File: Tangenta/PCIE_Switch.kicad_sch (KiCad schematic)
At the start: 99 parts, among them U15 PI7C9X2G404SLBFDEX, U17 M24C04-RMN6TP

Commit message: ...
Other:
- note removed: "Do not populate initially!"
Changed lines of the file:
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@@
     (effects (font (size 1.27 1.27)) (justify right bottom))
-  )
-  (text "Do not populate initially!" (at 27.305 196.215 0)
-    (effects (font (size 1.27 1.27)) (justify left bottom))
   )
   (text "|\n|\n|\n|" (at 295.91 139.7 0)

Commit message: Schematic improvements.
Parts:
- added J15: Conn_01x06_Pin, Connector_PinHeader_1.00mm:PinHeader_1x06_P1.00mm_Vertical, symbol Connector:Conn_01x06_Pin
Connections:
- net GNDREF: now also J15.1 (Pin_1)
- net PCIE_SW_TCK: now also J15.2 (Pin_2)
- net PCIE_SW_TDI: now also J15.3 (Pin_3)
- net PCIE_SW_TDO: now also J15.4 (Pin_4)
- net PCIE_SW_TMS: now also J15.5 (Pin_5)
- net PCIE_SW_TRST_L: now also J15.6 (Pin_6)
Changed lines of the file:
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@@
     (stroke (width 0) (type default))
   )
+  (wire (pts (xy 34.29 97.155) (xy 57.15 97.155))
+    (stroke (width 0) (type default))
+  )
   (wire (pts (xy 35.56 135.255) (xy 18.415 135.255))
     (stroke (width 0) (type default))
@@
     (stroke (width 0) (type default))
   )
+  (wire (pts (xy 34.29 102.235) (xy 57.15 102.235))
+    (stroke (width 0) (type default))
+  )
   (wire (pts (xy 382.905 223.52) (xy 400.05 223.52))
     (stroke (width 0) (type default))
@@
     (stroke (width 0) (type default))
   )
-  (wire (pts (xy 233.68 161.29) (xy 248.92 161.29))
+  (wire (pts (xy 34.29 99.695) (xy 57.15 99.695))
     (stroke (width 0) (type default))
   )
-  (wire (pts (xy 180.34 218.44) (xy 165.1 218.44))
+  (wire (pts (xy 233.68 161.29) (xy 248.92 161.29))
     (stroke (width 0) (type default))
   )
-  (wire (pts (xy 57.15 99.06) (xy 34.29 99.06))
+  (wire (pts (xy 180.34 218.44) (xy 165.1 218.44))
     (stroke (width 0) (type default))
   )
@@
     (stroke (width 0) (type default))
   )
-  (wire (pts (xy 57.15 91.44) (xy 34.29 91.44))
-    (stroke (width 0) (type default))
-  )
   (wire (pts (xy 363.22 93.98) (xy 363.22 96.52))
     (stroke (width 0) (type default))
@@
     (stroke (width 0) (type default))
   )
+  (wire (pts (xy 34.29 92.075) (xy 57.15 92.075))
+    (stroke (width 0) (type default))
+  )
   (wire (pts (xy 35.56 264.795) (xy 18.415 264.795))
     (stroke (width 0) (type default))
@@
     (stroke (width 0) (type default))
   )
-  (wire (pts (xy 57.15 93.98) (xy 34.29 93.98))
-    (stroke (width 0) (type default))
-  )
   (wire (pts (xy 379.73 115.57) (xy 379.73 118.11))
     (stroke (width 0) (type default))
@@
     (stroke (width 0) (type default))
   )
+  (wire (pts (xy 34.29 104.775) (xy 57.15 104.775))
+    (stroke (width 0) (type default))
+  )
   (wire (pts (xy 213.36 267.97) (xy 232.41 267.97))
     (stroke (width 0) (type default))
@@
     (stroke (width 0) (type default))
   )
-  (wire (pts (xy 57.15 101.6) (xy 34.29 101.6))
-    (stroke (width 0) (type default))
-  )
   (wire (pts (xy 18.415 177.165) (xy 35.56 177.165))
     (stroke (width 0) (type default))
@@
     (stroke (width 0) (type default))
   )
-  (wire (pts (xy 57.15 96.52) (xy 34.29 96.52))
-    (stroke (width 0) (type default))
-  )
   (wire (pts (xy 180.34 139.7) (xy 165.1 139.7))
     (stroke (width 0) (type default))
@@
     (stroke (width 0) (type default))
   )
+  (wire (pts (xy 34.29 94.615) (xy 57.15 94.615))
+    (stroke (width 0) (type default))
+  )
   (wire (pts (xy 389.89 22.86) (xy 389.89 25.4))
     (stroke (width 0) (type default))
@@
     (effects (font (size 1.27 1.27)) (justify right bottom))
   )
-  (label "PCIE_SW_TRST_L" (at 57.15 101.6 180) (fields_autoplaced)
+  (label "PCIE_SW_TRST_L" (at 57.15 104.775 180) (fields_autoplaced)
     (effects (font (size 1.27 1.27)) (justify right bottom))
   )
@@
     (effects (font (size 1.27 1.27)) (justify left bottom))
   )
+  (label "GND" (at 57.15 92.075 180) (fields_autoplaced)
+    (effects (font (size 1.27 1.27)) (justify right bottom))
+  )
   (label "1V0" (at 318.77 93.98 0) (fields_autoplaced)
     (effects (font (size 1.27 1.27)) (justify left bottom))
@@
     (effects (font (size 1.27 1.27)) (justify left bottom))
   )
-  (label "PCIE_SW_TCK" (at 57.15 91.44 180) (fields_autoplaced)
+  (label "PCIE_SW_TCK" (at 57.15 94.615 180) (fields_autoplaced)
     (effects (font (size 1.27 1.27)) (justify right bottom))
   )
@@
     (effects (font (size 1.27 1.27)) (justify left bottom))
   )
-  (label "PCIE_SW_TDO" (at 57.15 96.52 180) (fields_autoplaced)
+  (label "PCIE_SW_TDO" (at 57.15 99.695 180) (fields_autoplaced)
     (effects (font (size 1.27 1.27)) (justify right bottom))
   )
@@
     (effects (font (size 1.27 1.27)) (justify left bottom))
   )
-  (label "PCIE_SW_TMS" (at 57.15 99.06 180) (fields_autoplaced)
+  (label "PCIE_SW_TMS" (at 57.15 102.235 180) (fields_autoplaced)
     (effects (font (size 1.27 1.27)) (justify right bottom))
   )
@@
     (effects (font (size 1.27 1.27)) (justify left bottom))
   )
-  (label "PCIE_SW_TDI" (at 57.15 93.98 180) (fields_autoplaced)
+  (label "PCIE_SW_TDI" (at 57.15 97.155 180) (fields_autoplaced)
     (effects (font (size 1.27 1.27)) (justify right bottom))
   )
@@
     (effects (font (size 1.27 1.27)) (justify left bottom))
   )
-  (hierarchical_label "PCIE_SW_TDO" (shape input) (at 34.29 96.52 180) (fields_autoplaced)
-    (effects (font (size 1.27 1.27)) (justify right))
-  )
   (hierarchical_label "PCIE1_CLK_N" (shape output) (at 386.715 139.7 0) (fields_autoplaced)
     (effects (font (size 1.27 1.27)) (justify left))
@@
     (effects (font (size 1.27 1.27)) (justify left))
   )
-  (hierarchical_label "PCIE_SW_TCK" (shape input) (at 34.29 91.44 180) (fields_autoplaced)
-    (effects (font (size 1.27 1.27)) (justify right))
-  )
   (hierarchical_label "PCIE3_PRSNT" (shape output) (at 386.715 190.5 0) (fields_autoplaced)
     (effects (font (size 1.27 1.27)) (justify left))
@@
     (effects (font (size 1.27 1.27)) (justify left))
   )
-  (hierarchical_label "PCIE_SW_TMS" (shape input) (at 34.29 99.06 180) (fields_autoplaced)
-    (effects (font (size 1.27 1.27)) (justify right))
-  )
   (hierarchical_label "PCIE2_CLK_N" (shape output) (at 386.715 168.91 0) (fields_autoplaced)
     (effects (font (size 1.27 1.27)) (justify left))
@@
     (effects (font (size 1.27 1.27)) (justify left))
   )
-  (hierarchical_label "PCIE_SW_TDI" (shape input) (at 34.29 93.98 180) (fields_autoplaced)
-    (effects (font (size 1.27 1.27)) (justify right))
-  )
-  (hierarchical_label "PCIE_SW_TRST_L" (shape input) (at 34.29 101.6 180) (fields_autoplaced)
-    (effects (font (size 1.27 1.27)) (justify right))
-  )
   (hierarchical_label "PCIE_RX_P" (shape input) (at 34.29 73.66 180) (fields_autoplaced)
     (effects (font (size 1.27 1.27)) (justify right))
@@
         )
       )
+    )
+  )
+  (symbol (lib_id "Connector:Conn_01x06_Pin") (at 29.21 97.155 0) (unit 1)
+    (in_bom yes) (on_board yes) (dnp no)
+    (property "Reference" "J15" (at 26.289 98.298 0)
+      (effects (font (size 1.27 1.27)))
+    )
+    (property "Value" "Conn_01x06_Pin" (at 29.845 89.535 0)
+      (effects (font (size 1.27 1.27)) hide)
+    )
+    (property "Footprint" "Connector_PinHeader_1.00mm:PinHeader_1x06_P1.00mm_Vertical" (at 29.21 97.155 0)
+      (effects (font (size 1.27 1.27)) hide)
+    )
+    (property "Datasheet" "~" (at 29.21 97.155 0)
+      (effects (font (size 1.27 1.27)) hide)
+    )
+    (pin "1")
+    (pin "2")
+    (pin "3")
+    (pin "4")
+    (pin "5")
+    (pin "6")
+    (instances
+      (project "Tangenta"
+        (path "/358d1bcf-7599-4352-8c4d-baa18a5f09e6/db297b0b-35f2-4e86-892c-83973f1ac2db"
+          (reference "J15") (unit 1)
+        )
+        (path "/358d1bcf-7599-4352-8c4d-baa18a5f09e6/9b1f6f94-444c-4c59-8de9-290bde336856/04648235-6c5e-4915-ab80-8fea22048f3c"
+          (reference "J15") (unit 1)
+        )
+      )

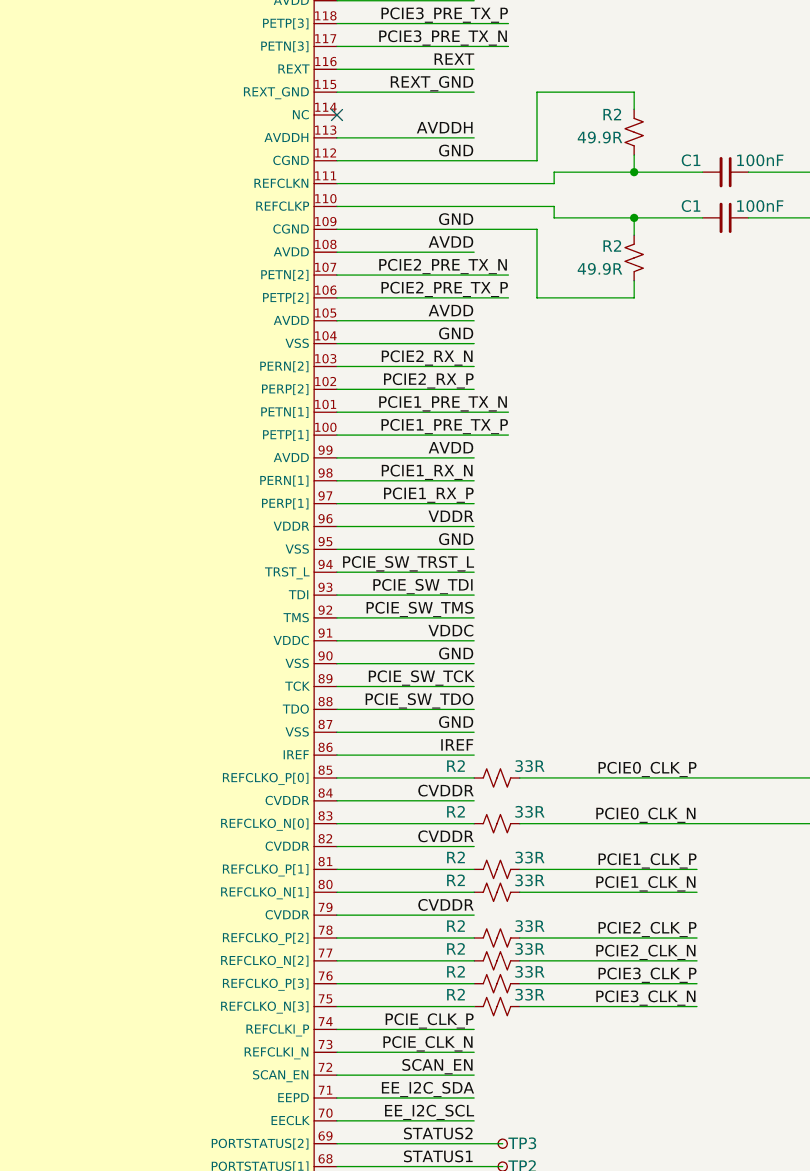
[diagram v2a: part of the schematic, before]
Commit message: Adding the remaining PCIe nets.
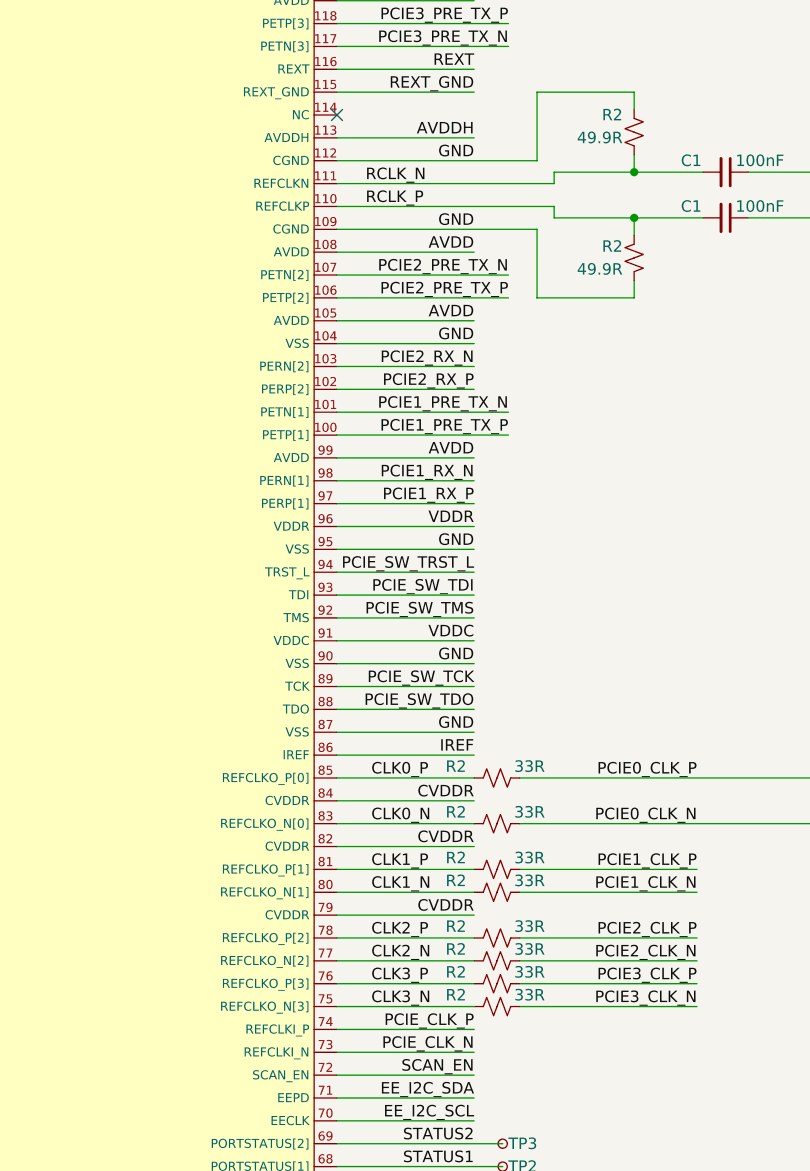
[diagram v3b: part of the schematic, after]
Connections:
- net RCLK_P: now reaches C1.2, R2.1, U15.110 (REFCLKP)
- net RCLK_N: now reaches C1.2, R2.1, U15.111 (REFCLKN)
- net CLK3_N: now reaches R2.2, U15.75 (REFCLKO_N[3])
- net CLK3_P: now reaches R2.2, U15.76 (REFCLKO_P[3])
- net CLK2_N: now reaches R2.2, U15.77 (REFCLKO_N[2])
- net CLK2_P: now reaches R2.2, U15.78 (REFCLKO_P[2])
- net CLK1_N: now reaches R2.2, U15.80 (REFCLKO_N[1])
- net CLK1_P: now reaches R2.2, U15.81 (REFCLKO_P[1])
- net CLK0_N: now reaches R2.2, U15.83 (REFCLKO_N[0])
- net CLK0_P: now reaches R2.2, U15.85 (REFCLKO_P[0])
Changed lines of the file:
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@@
+    (effects (font (size 1.27 1.27)) (justify left bottom))
+  )
+  (label "CLK1_N" (at 237.49 181.61 0) (fields_autoplaced)
     (effects (font (size 1.27 1.27)) (justify left bottom))
   )
@@
     (effects (font (size 1.27 1.27)) (justify right bottom))
   )
+  (label "CLK0_P" (at 237.49 168.91 0) (fields_autoplaced)
+    (effects (font (size 1.27 1.27)) (justify left bottom))
+  )
   (label "GND" (at 248.92 100.33 180) (fields_autoplaced)
     (effects (font (size 1.27 1.27)) (justify right bottom))
@@
     (effects (font (size 1.27 1.27)) (justify right bottom))
   )
+  (label "CLK2_P" (at 237.49 186.69 0) (fields_autoplaced)
+    (effects (font (size 1.27 1.27)) (justify left bottom))
+  )
   (label "GND" (at 165.1 134.62 0) (fields_autoplaced)
     (effects (font (size 1.27 1.27)) (justify left bottom))
   )
+  (label "CLK2_N" (at 237.49 189.23 0) (fields_autoplaced)
+    (effects (font (size 1.27 1.27)) (justify left bottom))
+  )
   (label "TEST2" (at 18.415 177.165 0) (fields_autoplaced)
     (effects (font (size 1.27 1.27)) (justify left bottom))
@@
     (effects (font (size 1.27 1.27)) (justify left bottom))
   )
+  (label "CLK1_P" (at 237.49 179.07 0) (fields_autoplaced)
+    (effects (font (size 1.27 1.27)) (justify left bottom))
+  )
   (label "GND" (at 165.1 88.9 0) (fields_autoplaced)
     (effects (font (size 1.27 1.27)) (justify left bottom))
@@
     (effects (font (size 1.27 1.27)) (justify left bottom))
   )
+  (label "CLK3_N" (at 237.49 194.31 0) (fields_autoplaced)
+    (effects (font (size 1.27 1.27)) (justify left bottom))
+  )
   (label "GND" (at 57.785 180.34 180) (fields_autoplaced)
     (effects (font (size 1.27 1.27)) (justify right bottom))
@@
     (effects (font (size 1.27 1.27)) (justify left bottom))
   )
+  (label "RCLK_N" (at 236.855 102.87 0) (fields_autoplaced)
+    (effects (font (size 1.27 1.27)) (justify left bottom))
+  )
   (label "SCAN_EN" (at 248.92 201.93 180) (fields_autoplaced)
     (effects (font (size 1.27 1.27)) (justify right bottom))
@@
     (effects (font (size 1.27 1.27)) (justify left bottom))
   )
+  (label "RCLK_P" (at 236.855 105.41 0) (fields_autoplaced)
+    (effects (font (size 1.27 1.27)) (justify left bottom))
+  )
   (label "PCIE_SW_TCK" (at 57.15 94.615 180) (fields_autoplaced)
     (effects (font (size 1.27 1.27)) (justify right bottom))
@@
     (effects (font (size 1.27 1.27)) (justify left bottom))
   )
+  (label "CLK0_N" (at 237.49 173.99 0) (fields_autoplaced)
+    (effects (font (size 1.27 1.27)) (justify left bottom))
+  )
   (label "PCIE3_PRE_TX_N" (at 179.705 267.97 0) (fields_autoplaced)
     (effects (font (size 1.27 1.27)) (justify left bottom))
@@
     (effects (font (size 1.27 1.27)) (justify right bottom))
   )
+  (label "CLK3_P" (at 237.49 191.77 0) (fields_autoplaced)
+    (effects (font (size 1.27 1.27)) (justify left bottom))
+  )
   (label "PCIE1_PRSNT" (at 370.205 130.81 0) (fields_autoplaced)

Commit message: PCIe switch fanout, in progress...
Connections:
- net PCIE_SW_TCK: now also J15.5 (Pin_5); no longer J15.2 (Pin_2)
- net PCIE_SW_TDO: now also J15.6 (Pin_6); no longer J15.4 (Pin_4)
- net PCIE_SW_TMS: now also J15.4 (Pin_4); no longer J15.5 (Pin_5)
- net PCIE_SW_TRST_L: now also J15.2 (Pin_2); no longer J15.6 (Pin_6)
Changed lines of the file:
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@@
     (effects (font (size 1.27 1.27)) (justify right bottom))
   )
-  (label "PCIE_SW_TRST_L" (at 57.15 104.775 180) (fields_autoplaced)
+  (label "PCIE_SW_TRST_L" (at 57.15 94.615 180) (fields_autoplaced)
     (effects (font (size 1.27 1.27)) (justify right bottom))
   )
@@
     (effects (font (size 1.27 1.27)) (justify left bottom))
   )
-  (label "PCIE_SW_TCK" (at 57.15 94.615 180) (fields_autoplaced)
+  (label "PCIE_SW_TCK" (at 57.15 102.235 180) (fields_autoplaced)
     (effects (font (size 1.27 1.27)) (justify right bottom))
   )
@@
     (effects (font (size 1.27 1.27)) (justify left bottom))
   )
-  (label "PCIE_SW_TDO" (at 57.15 99.695 180) (fields_autoplaced)
+  (label "PCIE_SW_TDO" (at 57.15 104.775 180) (fields_autoplaced)
     (effects (font (size 1.27 1.27)) (justify right bottom))
   )
@@
     (effects (font (size 1.27 1.27)) (justify left bottom))
   )
-  (label "PCIE_SW_TMS" (at 57.15 102.235 180) (fields_autoplaced)
-    (effects (font (size 1.27 1.27)) (justify right bottom))
-  )
+  (label "PCIE_SW_TMS" (at 57.15 99.695 180) (fields_autoplaced)
+    (effects (font (size 1.27 1.27)) (justify right bottom))
+  )

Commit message: Libraries exported from global to project.
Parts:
- C1: symbol Device:C_Small -> CholaSymbolsPrjLib:C_Small
- J15: symbol Connector:Conn_01x06_Pin -> CholaSymbolsPrjLib:Conn_01x06_Pin
- R2: symbol Device:R_Small_US -> CholaSymbolsPrjLib:R_Small_US
- TP1, TP2, TP3: symbol Connector:TestPoint_Small -> CholaSymbolsPrjLib:TestPoint_Small
- U15: symbol PCIE_Switch:PI7C9X2G404SLBFDEX -> CholaSymbolsPrjLib:PI7C9X2G404SLBFDEX
- U17: symbol M24C04-RMN6TP:M24C04-RMN6TP -> CholaSymbolsPrjLib:M24C04-RMN6TP

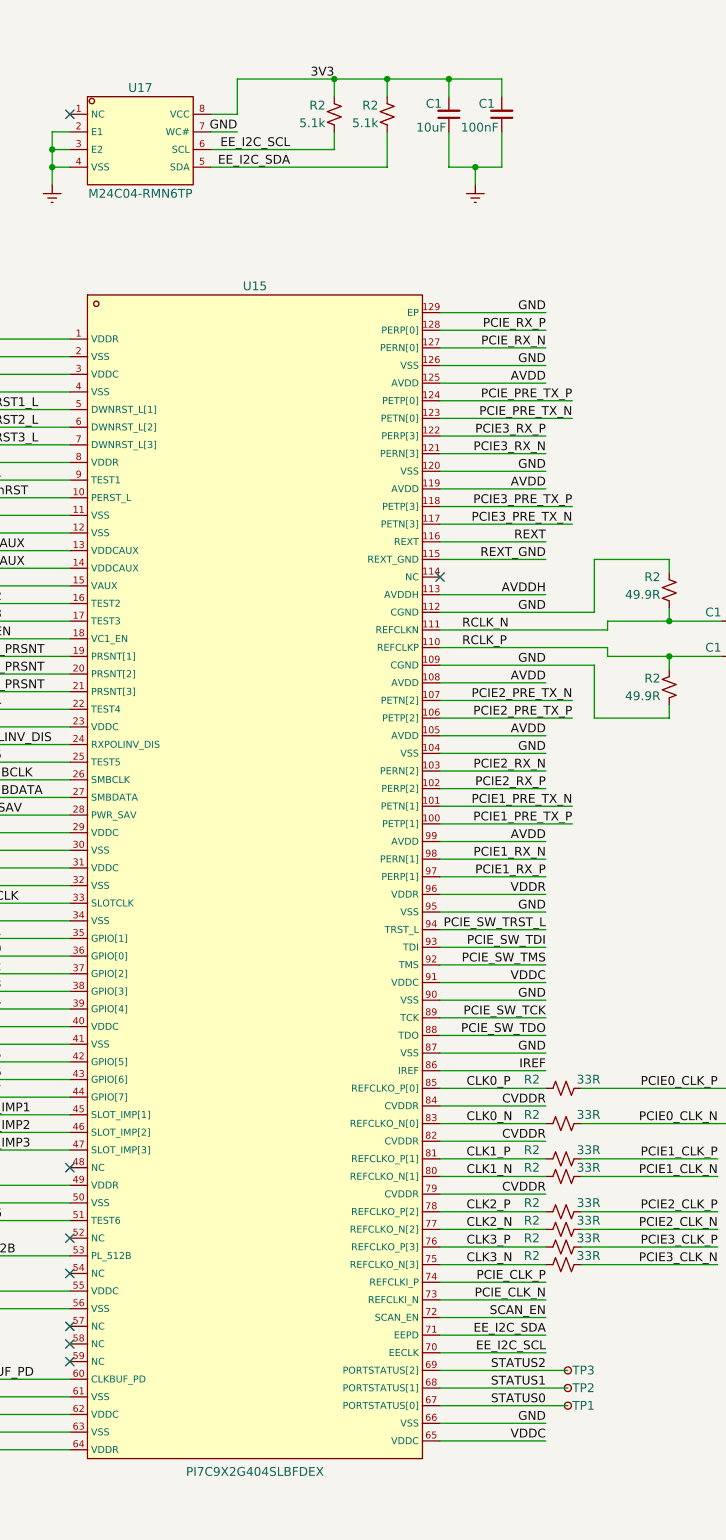
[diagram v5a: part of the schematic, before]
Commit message: Re-annotated. Ready for JLCPCB design verification.
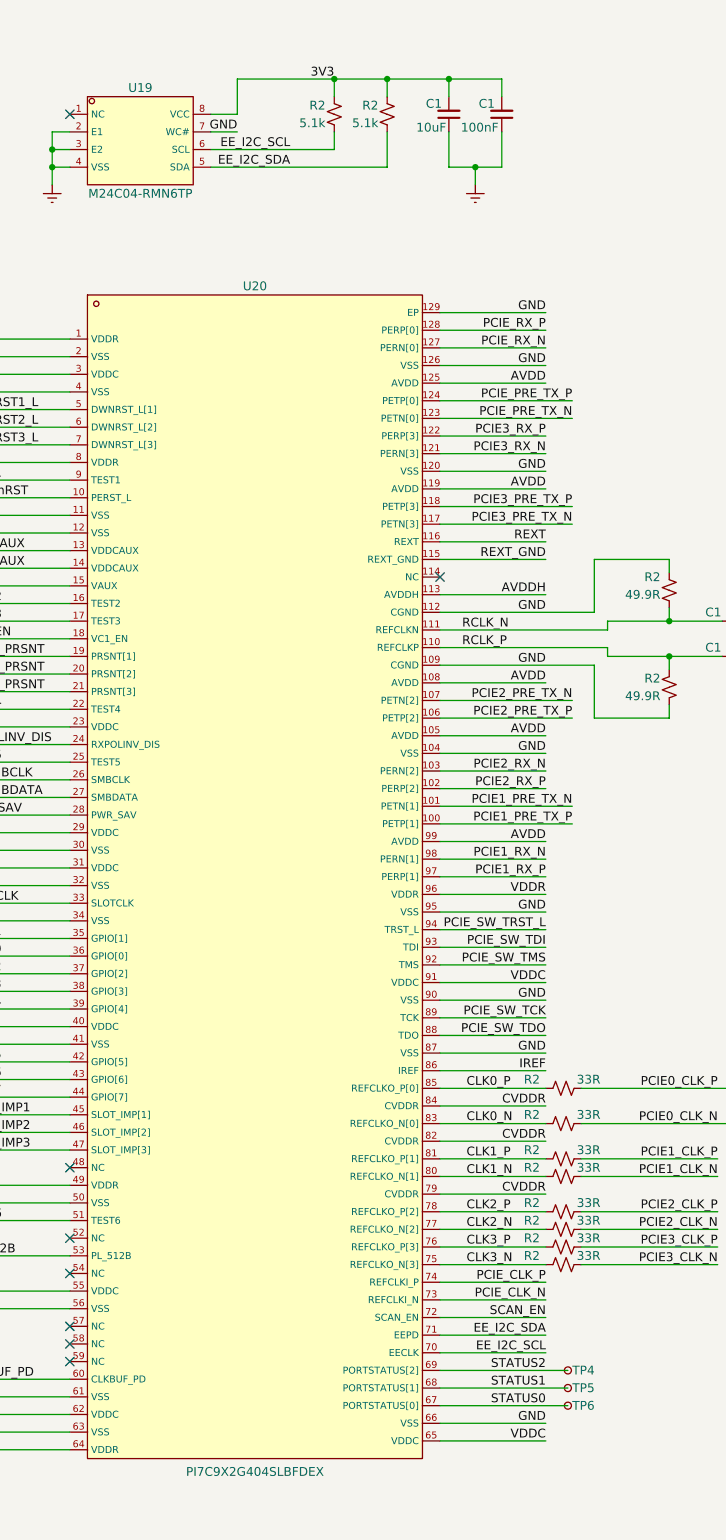
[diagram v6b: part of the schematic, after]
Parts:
- renumbered TP3 to TP4, TP2 to TP5, TP1 to TP6, U17 to U19, U15 to U20

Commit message: ...
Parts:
- C1: symbol CholaSymbolsPrjLib:C_Small -> LocalPrjLib:C_Small
- J15: symbol CholaSymbolsPrjLib:Conn_01x06_Pin -> LocalPrjLib:Conn_01x06_Pin
- R2: symbol CholaSymbolsPrjLib:R_Small_US -> LocalPrjLib:R_Small_US
- TP4, TP5, TP6: symbol CholaSymbolsPrjLib:TestPoint_Small -> LocalPrjLib:TestPoint_Small
- U19: symbol CholaSymbolsPrjLib:M24C04-RMN6TP -> LocalPrjLib:M24C04-RMN6TP
- U20: symbol CholaSymbolsPrjLib:PI7C9X2G404SLBFDEX -> LocalPrjLib:PI7C9X2G404SLBFDEX

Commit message: Fixes, new approach.
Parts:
- C1: symbol LocalPrjLib:C_Small -> LocalSymbolsPrjLib:C_Small
- J15: symbol LocalPrjLib:Conn_01x06_Pin -> LocalSymbolsPrjLib:Conn_01x06_Pin
- R2: symbol LocalPrjLib:R_Small_US -> LocalSymbolsPrjLib:R_Small_US
- TP4, TP5, TP6: symbol LocalPrjLib:TestPoint_Small -> LocalSymbolsPrjLib:TestPoint_Small
- U19: symbol LocalPrjLib:M24C04-RMN6TP -> LocalSymbolsPrjLib:M24C04-RMN6TP
- U20: symbol LocalPrjLib:PI7C9X2G404SLBFDEX -> LocalSymbolsPrjLib:PI7C9X2G404SLBFDEX
